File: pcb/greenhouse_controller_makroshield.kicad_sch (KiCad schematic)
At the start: 0 parts

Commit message: WIP, add conntectors
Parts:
- added C?: CAP_CER_22UF_10V_0603, connaxio-capacitors:CAP_CER_0603_1608M, symbol connaxio-capacitors:CAP_CER_22UF_10V_0603
- added D?: DIO_SBD_100V_3A_SMA, connaxio-diodes:DO-214AC_SMA, symbol connaxio-diodes:DIO_SBD_100V_3A_SMA
- added D?: DIO_TVS_24V_UNI_SMA, connaxio-diodes:DO-214AC_SMA, symbol connaxio-diodes:DIO_TVS_24V_UNI_SMA
- added J?: CON_HDR_MIKROBUS_ADDON_TH, connaxio-connectors:CON_HDR_MIKROBUS_ADDON_TH, symbol connaxio-connectors:CON_HDR_MIKROBUS_ADDON_TH
- added J?: CON_TERM_BLK_1X2_TB008A-508-02BE, connaxio-connectors:CON_TERM_BLK_1X2_TB008A-508-02BE, symbol connaxio-connectors:CON_TERM_BLK_1X2_TB008A-508-02BE
- added U?: CON_BARREL_2.1X5.5_PJ-002A, connaxio-connectors:CON_BARREL_2.1X5.5_PJ-002A, symbol connaxio-connectors:CON_BARREL_2.1X5.5_PJ-002A
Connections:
- new net: D?.2 (A), U?.1
- new net: D?.1 (K), J?.1
- new net +3.3V: J?.7 (+3.3V)
- new net +5V: C?.1, D?.1 (K), J?.15 (+5V)
- new net GND: C?.2, D?.2 (A), J?.16 (GND), J?.2, J?.8 (GND), U?.2, U?.3
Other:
- note added: "24 V AC or DC outputs (MOSFET & caps or TRIAC, TVS diode, Freewheeling diode)"
- note added: "24 VAC PSU Input (TBC) (TVS diode)"
- note added: "24 VDC Motor outputs (H-Bridge, PTC, connector, freewheeling diodes if necessary))"
- note added: "24 VDC PSU Input (Ideal diode, TVS diode, caps)"
- note added: "5 VDC input"
- note added: "Logic conditioning"
- note added: "mikroBUS add-on header (controller)"

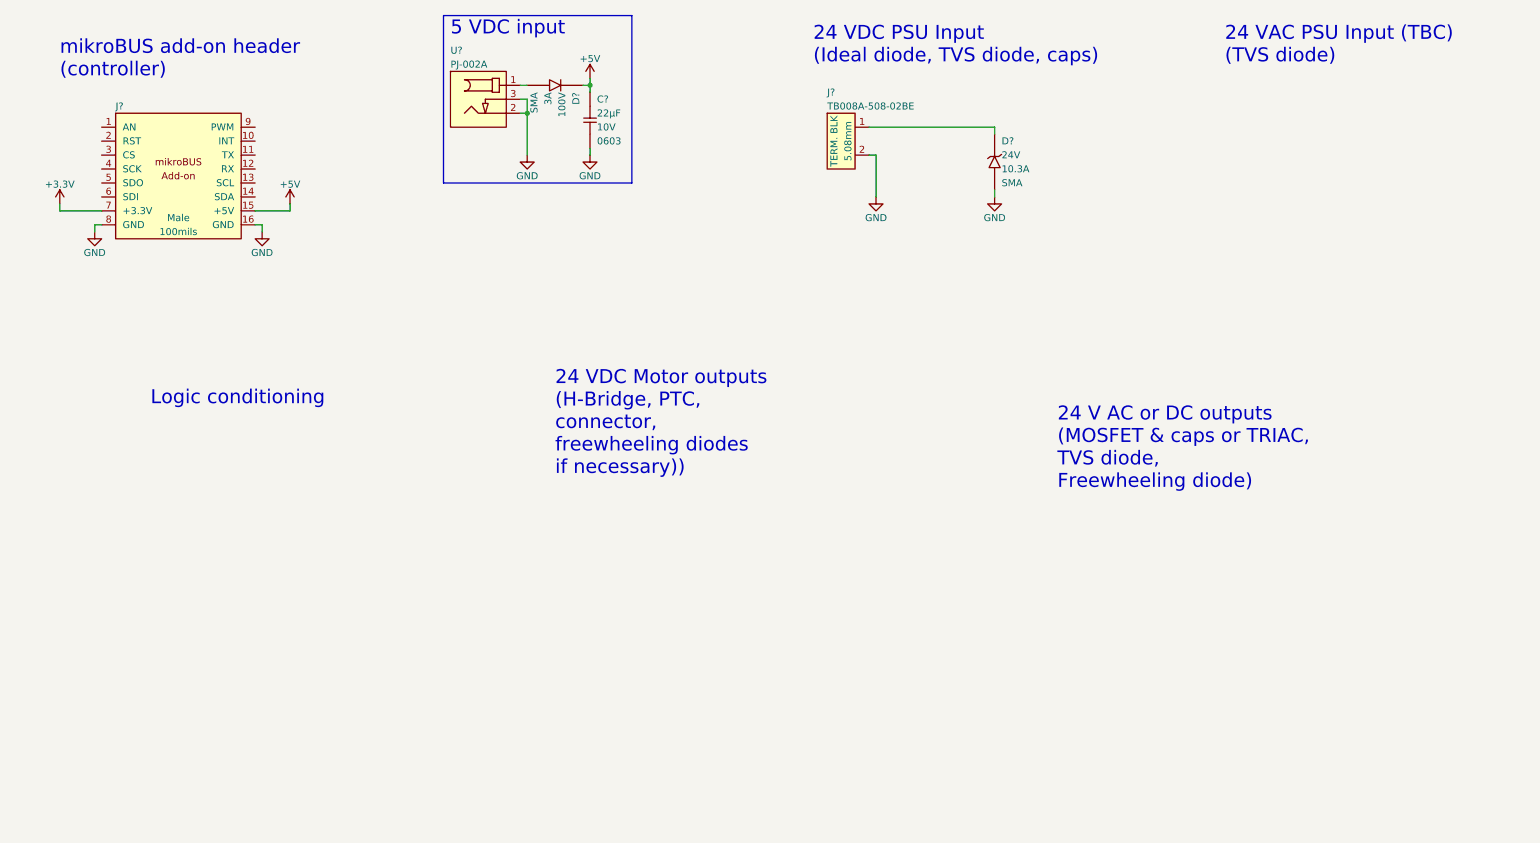
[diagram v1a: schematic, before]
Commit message: Finish 24VDC input
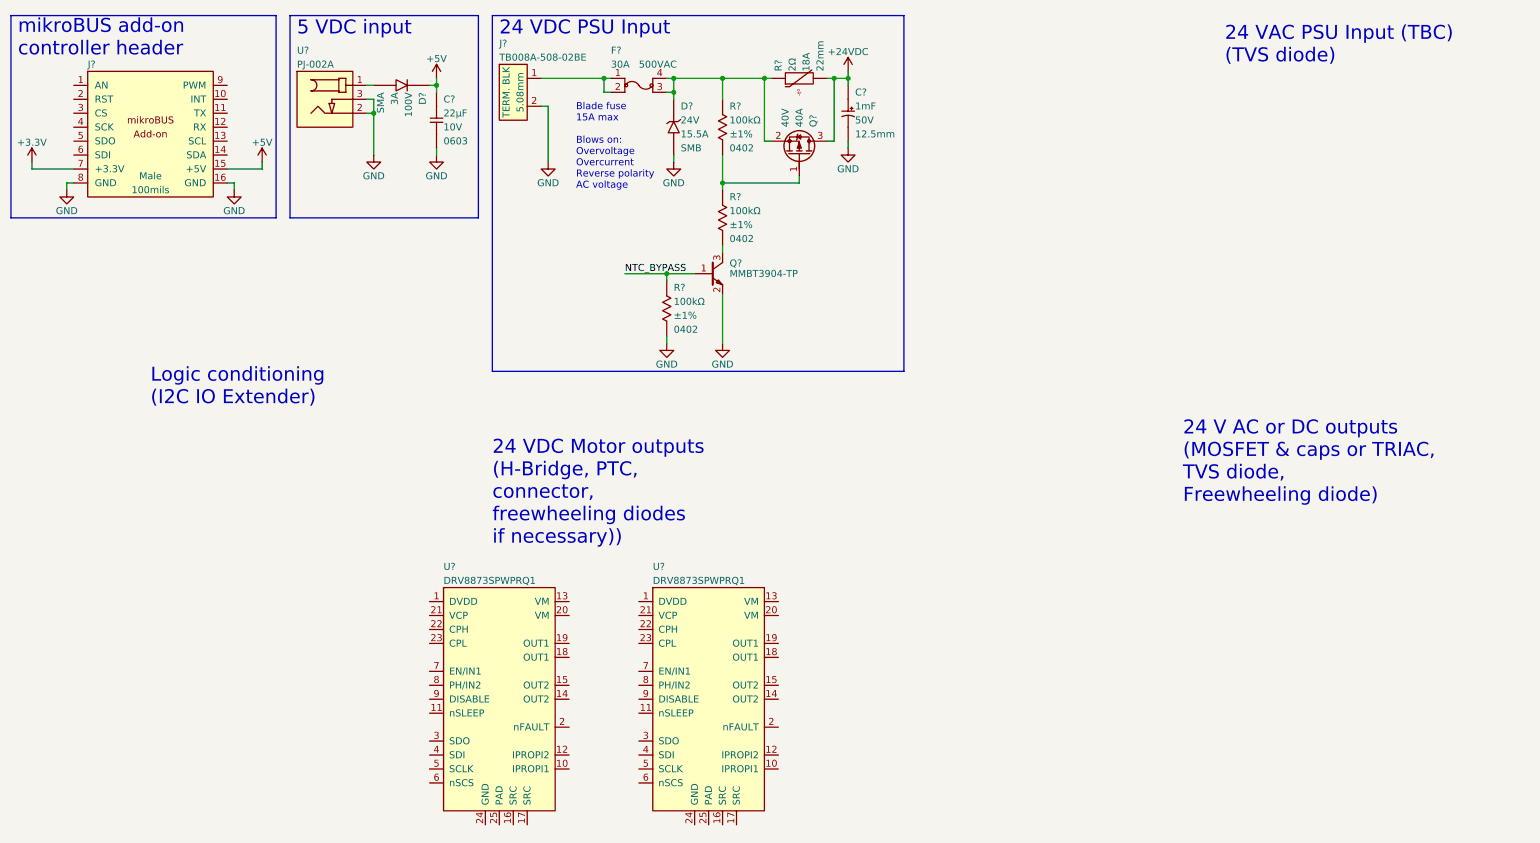
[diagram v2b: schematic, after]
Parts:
- removed D?: DIO_TVS_24V_UNI_SMA, connaxio-diodes:DO-214AC_SMA, symbol connaxio-diodes:DIO_TVS_24V_UNI_SMA
- added C?: CAP_AE_1MF_50V_TH_12.5MM, connaxio-capacitors:CAPAE_RAD_D12.5_H26.5_P5, symbol connaxio-capacitors:CAP_AE_1MF_50V_TH_12.5MM
- added D?: DIO_TVS_24V_UNI_SMB, connaxio-diodes:DO-124AA_SMB, symbol connaxio-diodes:DIO_TVS_24V_UNI_SMB
- added F?: FUS_BLADE_3522, connaxio-connectors:FUS_BLADE_3522, symbol connaxio-connectors:FUS_BLADE_3522
- added Q?: TRX_NPN_MMBT3904-TP, connaxio-sop:SOT-23-3, symbol connaxio-transistors:TRX_NPN_MMBT3904-TP
- added Q?: TRX_PMOS_AOD4189, connaxio-sop:TO-252-3, symbol connaxio-transistors:TRX_PMOS_AOD4189
- added R? (x3): RES_100KΩ_1%_0402, connaxio-resistors:RES_0402_1005M, symbol connaxio-resistors:RES_100KΩ_1%_0402
- added R?: NTC_SL22 2R018, connaxio-resistors:RV_DISC_D22_W6_P7.8, symbol connaxio-resistors:NTC_SL22 2R018
- added U? (x2): DRV_DRV8873SPWPRQ1, connaxio-sop:TSSOP-24_4.4x7.8_P0.65_EP3.2x5.26, symbol connaxio-ic:DRV_DRV8873SPWPRQ1
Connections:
- net GND: now also C?.2, D?.2 (A), Q?.2 (E), R?.2
- net at J?.1: now also F?.1, F?.2
- new net: D?.1 (K), F?.3, F?.4, Q?.2 (S), R?.1, R?.1
- new net: Q?.1 (G), R?.1, R?.2
- new net: Q?.3 (C), R?.2
- new net +24VDC: C?.1, Q?.3 (D), R?.2
- new net NTC_BYPASS: Q?.1 (B), R?.1
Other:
- note added: "24 VDC PSU Input"
- note added: "Blade fuse 15A max Blows on: Overvoltage Overcurrent Reverse polarity AC voltage"
- note added: "Logic conditioning (I2C IO Extender)"
- note added: "mikroBUS add-on controller header"
- note removed: "24 VDC PSU Input (Ideal diode, TVS diode, caps)"
- note removed: "Logic conditioning"
- note removed: "mikroBUS add-on header (controller)"
- moved on the sheet: C?, D?, J?, U?

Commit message: Finish motor driver and add tentative switched output (TBC with valves)
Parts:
- removed U?: DRV_DRV8873SPWPRQ1, connaxio-sop:TSSOP-24_4.4x7.8_P0.65_EP3.2x5.26, symbol connaxio-ic:DRV_DRV8873SPWPRQ1
- added C? (x2): CAP_CER_2.2UF_25V_0402, connaxio-capacitors:CAP_CER_0402_1005M, symbol connaxio-capacitors:CAP_CER_2.2UF_25V_0402
- added C? (x2): CAP_AE_22UF_100V_TH_6.3MM, connaxio-capacitors:CAP_AE_RAD_D6.3_H12.5_P2.5, symbol connaxio-capacitors:CAP_AE_22UF_100V_TH_6.3MM
- added C? (x2): CAP_CER_100NF_25V_0402, connaxio-capacitors:CAP_CER_0402_1005M, symbol connaxio-capacitors:CAP_CER_100NF_25V_0402
- added C?: CAP_CER_47NF_25V_0402, connaxio-capacitors:CAP_CER_0402_1005M, symbol connaxio-capacitors:CAP_CER_47NF_25V_0402
- added F? (x4): FID_1X3, connaxio-mechanical:FID_1X3, symbol connaxio-mechanical:FID_1X3
- added F? (x2): FUS_BLADE_3522, connaxio-connectors:FUS_BLADE_3522, symbol connaxio-connectors:FUS_BLADE_3522
- added MTH? (x3): MTH_M2.5_NPTH, connaxio-mechanical:MTH_M2.5_NPTH, symbol connaxio-mechanical:MTH_M2.5_NPTH
- added MTH?: MTH_M2.5_PTH_CORNER, connaxio-mechanical:MTH_M2.5_PTH_CORNER, symbol connaxio-mechanical:MTH_M2.5_PTH_CORNER
- added Q?: TRX_PMOS_AOD4189, connaxio-sop:TO-252-3, symbol connaxio-transistors:TRX_PMOS_AOD4189
- added Q?: TRX_NPN_MMBT3904-TP, connaxio-sop:SOT-23-3, symbol connaxio-transistors:TRX_NPN_MMBT3904-TP
- added R? (x6): RES_1.54KΩ_1%_0402, connaxio-resistors:RES_0402_1005M, symbol connaxio-resistors:RES_1.54KΩ_1%_0402
- added R? (x2): RES_226Ω_1%_0402, connaxio-resistors:RES_0402_1005M, symbol connaxio-resistors:RES_226Ω_1%_0402
- added R?: RES_100KΩ_1%_0402, connaxio-resistors:RES_0402_1005M, symbol connaxio-resistors:RES_100KΩ_1%_0402
- added R?: RES_0Ω_0402, connaxio-resistors:RES_0402_1005M, symbol connaxio-resistors:RES_0Ω_0402
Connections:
- net +24VDC: now also F?.1, F?.2, F?.3, F?.4
- net +3.3V: now also U?.11 (nSLEEP), R?.1, R?.1
- net GND: now also U?.16 (SRC), U?.17 (SRC), U?.24 (GND), U?.25 (PAD), C?.2, C?.2, C?.2, C?.2, C?.2, Q?.2 (E), R?.2, R?.2, R?.2, R?.2
- net NTC_BYPASS: now also R?.1; no longer Q?.1 (B)
- net I2C_SCL: now reaches J?.13 (SCL)
- net I2C_SCL: now also R?.2
- net I2C_SDA: now reaches J?.14 (SDA)
- net I2C_SDA: now also R?.2
- net SPI_CS2: now reaches J?.2 (RST)
- net SPI_CS1: now reaches J?.3 (CS)
- net SPI_CS1: now also U?.6 (nSCS)
- net SPI_CK: now reaches J?.4 (SCK)
- net SPI_CK: now also U?.5 (SCLK)
- net SPI_DO: now reaches J?.5 (SDO)
- net SPI_DO: now also U?.4 (SDI)
- net SPI_DI: now reaches J?.6 (SDI)
- net SPI_DI: now also U?.3 (SDO)
- net SPI_CS3: now reaches J?.9 (PWM)
- net at U?.1 (DVDD): now also C?.1
- net at U?.10 (IPROPI1): now also R?.1
- net at U?.12 (IPROPI2): now also R?.1
- net at U?.13 (VM): now also U?.20 (VM), C?.1, C?.1, C?.2, F?.1, F?.2
- net M1_OUT2: now reaches U?.14 (OUT2)
- net M1_OUT2: now also U?.15 (OUT2)
- net M1_OUT1: now reaches U?.18 (OUT1)
- net M1_OUT1: now also U?.19 (OUT1)
- net at U?.21 (VCP): now also C?.1
- net at U?.22 (CPH): now also C?.1
- net at U?.23 (CPL): now also C?.2
- net M1_EN: now reaches U?.7 (EN/IN1)
- net M1_PH: now reaches U?.8 (PH/IN2)
- net M1_DIS: now reaches U?.9 (DISABLE)
- new net: C?.1, C?.1, F?.3, F?.4, Q?.2 (S), R?.1
- new net: Q?.1 (G), R?.1, R?.2
- new net: Q?.3 (C), R?.2
- new net: Q?.1 (B), R?.2 (x2)
- new net: MTH?.1, R?.1
- new net OUT1: Q?.3 (D)
- new net OUT1_EN: R?.1, R?.1
- no-connect marks 0 -> 1
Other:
- note added: "24 VDC motor 1"
- note added: "24 VDC switched output"
- note added: "Fiducials"
- note added: "Fuse depending on device [Max 15 A]"
- note added: "Fuse depending on motor [Max 10 A]"
- note added: "Mounting holes"
- note removed: "24 V AC or DC outputs (MOSFET & caps or TRIAC, TVS diode, Freewheeling diode)"
- note removed: "24 VDC Motor outputs (H-Bridge, PTC, connector, freewheeling diodes if necessary))"
- moved on the sheet: C?, D?, F?, J?, Q?, R?, U?
